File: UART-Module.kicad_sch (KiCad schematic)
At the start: 10 parts, among them J4 DE9_Receptacle_MountingHoles, Q2 1.8432, U1 74HC02, U2 74HC21, U3 W65C21N, U5 R65C51

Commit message: revise components
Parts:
- removed C1: 1uF, Capacitor_SMD:C_0805_2012Metric, symbol Device:C
- removed U3: W65C21N, Package_DIP:DIP-40_W15.24mm, symbol Interface:6821

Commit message: complete traces
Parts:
- C1: renamed from C2; footprint Capacitor_SMD:C_0805_2012Metric -> Capacitor_SMD:C_0805_2012Metric_Pad1.18x1.45mm_HandSolder
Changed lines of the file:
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@@
   (symbol (lib_id "Device:C") (at 118.11 129.54 270) (unit 1)
     (in_bom yes) (on_board yes) (dnp no) (fields_autoplaced)
-    (property "Reference" "C2" (at 118.11 122.174 90)
+    (property "Reference" "C1" (at 118.11 122.174 90)
       (effects (font (size 1.27 1.27)))
     )
@@
       (effects (font (size 1.27 1.27)))
     )
-    (property "Footprint" "Capacitor_SMD:C_0805_2012Metric" (at 114.3 130.5052 0)
+    (property "Footprint" "Capacitor_SMD:C_0805_2012Metric_Pad1.18x1.45mm_HandSolder" (at 114.3 130.5052 0)
       (effects (font (size 1.27 1.27)) hide)
     )
@@
       (project "UART-Module"
         (path "/1f20a268-715c-40e1-b980-8678b0e31942"
-          (reference "C2") (unit 1)
+          (reference "C1") (unit 1)
         )
       )
@@
       (project "UART-Module"
         (path "/1f20a268-715c-40e1-b980-8678b0e31942"
-          (reference "C3") (unit 1)
-        )
-      )
+          (reference "C2") (unit 1)
+        )
+      )

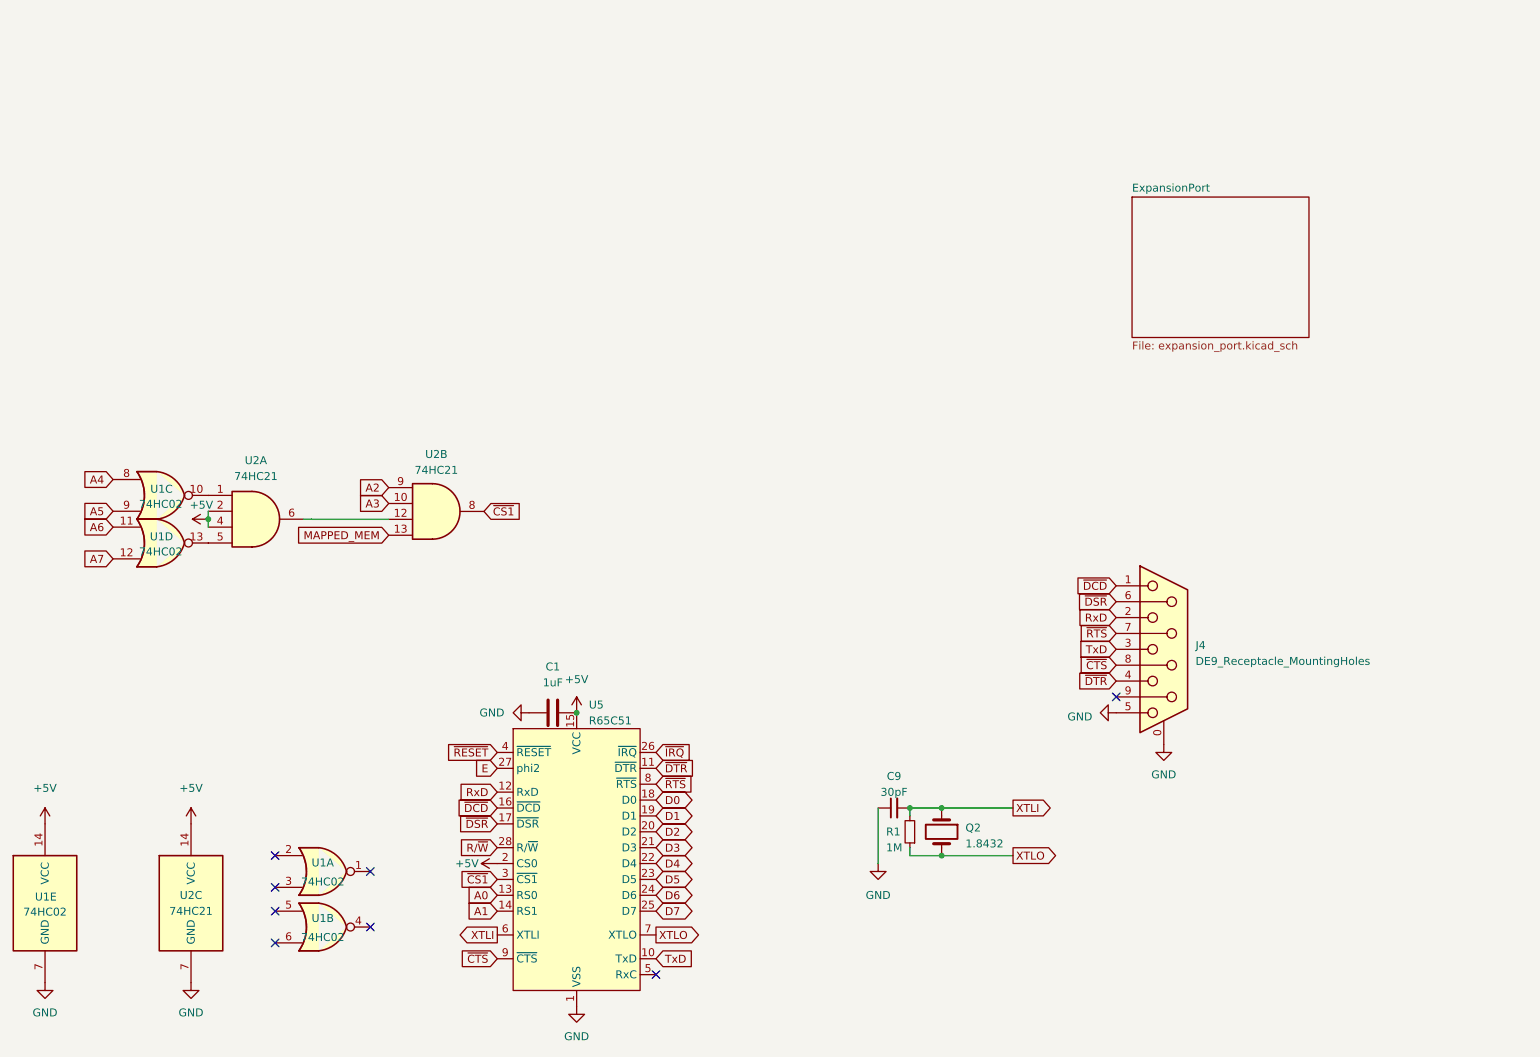
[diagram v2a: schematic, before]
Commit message: fix chip select
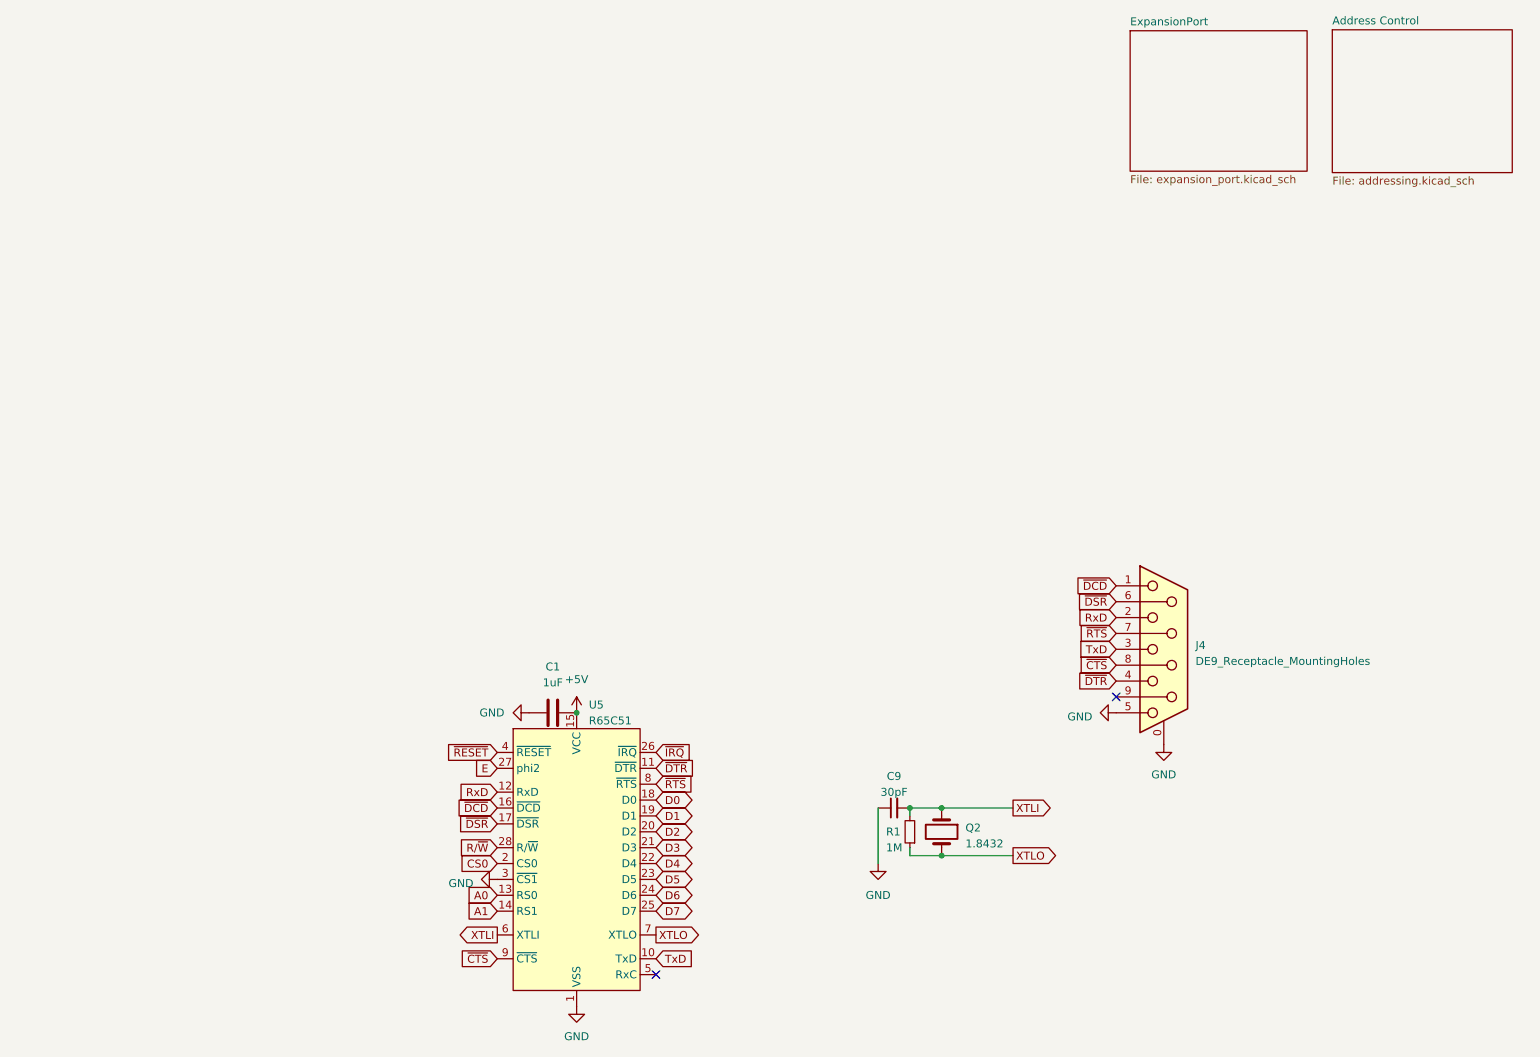
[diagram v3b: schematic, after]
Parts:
- removed U1: 74HC02, Package_SO:SO-14_3.9x8.65mm_P1.27mm, symbol 74xx:74LS02
- removed U2: 74HC21, Package_SO:SO-14_3.9x8.65mm_P1.27mm, symbol 74xx:74LS21
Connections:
- net ~{CS1} is gone; now on net GND: U5.3 (~{CS1})
- net +5V: no longer U5.2 (CS0)
- new net CS0: U5.2 (CS0)
- no-connect marks 8 -> 2
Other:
- added sheet Address Control (addressing.kicad_sch)

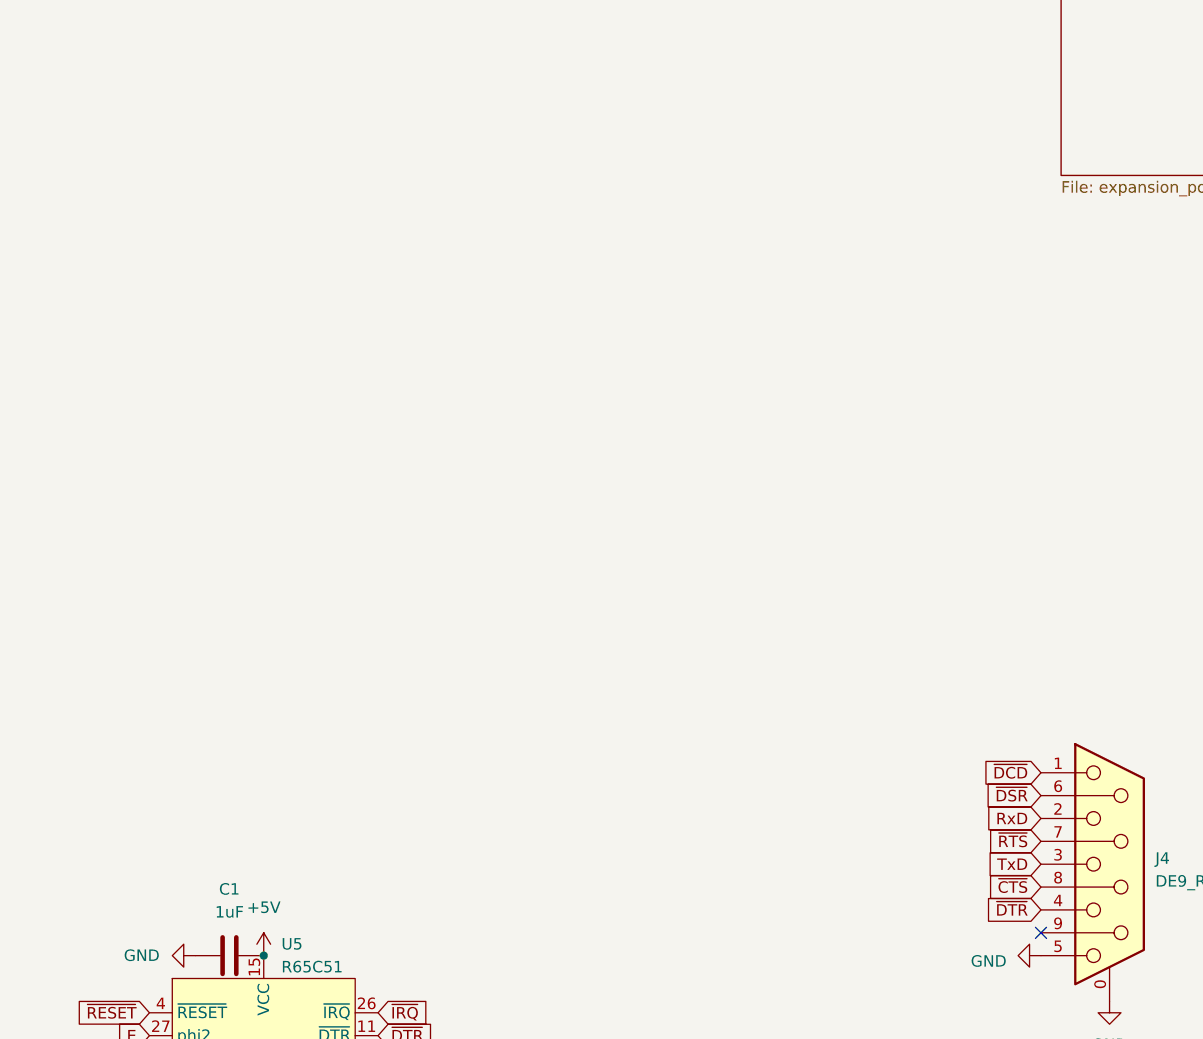
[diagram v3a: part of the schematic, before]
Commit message: add max232 for correct serial voltages
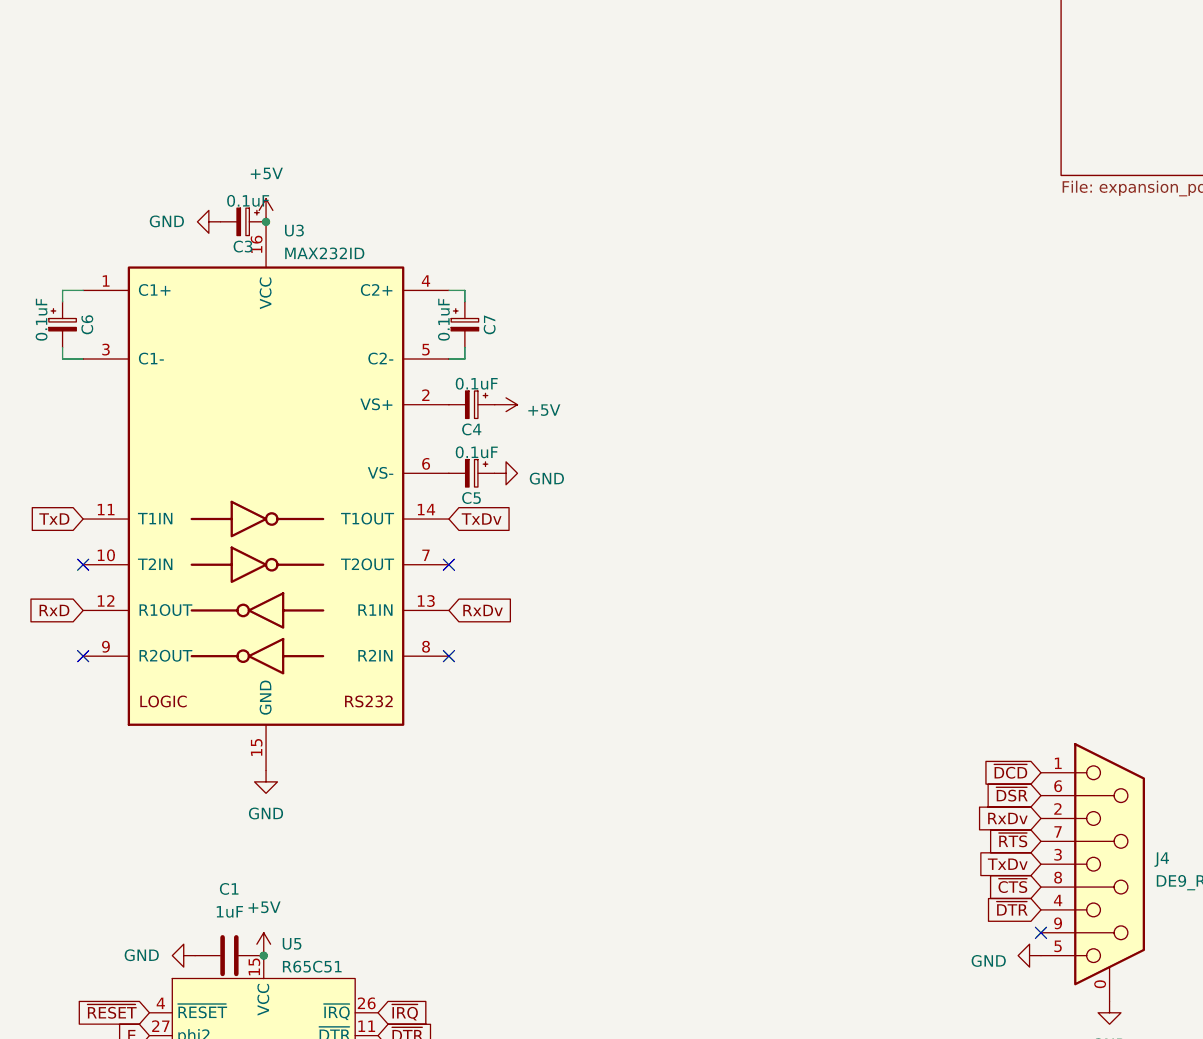
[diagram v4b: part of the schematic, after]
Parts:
- added C3, C4, C5, C6, C7: 0.1uF, Capacitor_THT:CP_Radial_Tantal_D4.5mm_P5.00mm, symbol Device:C_Polarized_Small
- added U3: MAX232ID, Package_SO:SOIC-16W_7.5x10.3mm_P1.27mm, symbol Interface_UART:MAX232
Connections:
- net +5V: now also C3.1, C4.1, U3.16 (VCC)
- net GND: now also C3.2, C5.1, U3.15 (GND)
- net RxD: now also U3.12 (R1OUT); no longer J4.2
- net TxD: now also U3.11 (T1IN); no longer J4.3
- new net: C6.1, U3.1 (C1+)
- new net: C6.2, U3.3 (C1-)
- new net: C4.2, U3.2 (VS+)
- new net: C7.1, U3.4 (C2+)
- new net: C7.2, U3.5 (C2-)
- new net: C5.2, U3.6 (VS-)
- new net RxDv: J4.2, U3.13 (R1IN)
- new net TxDv: J4.3, U3.14 (T1OUT)
- no-connect marks 2 -> 6

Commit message: fix footprint for U3
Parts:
- U3: footprint Package_SO:SOIC-16W_7.5x10.3mm_P1.27mm -> Package_SO:SOIC-16_4.55x10.3mm_P1.27mm
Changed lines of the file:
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@@
 (kicad_sch (version 20230121) (generator eeschema)
   (paper "A4")
+  (title_block
+    (date "2023-05-02")
+    (rev "1.2")
+  )
   (junction (at 121.92 129.54) (diameter 0) (color 0 0 0 0)
   )
@@
       (effects (font (size 1.27 1.27)) (justify left))
     )
-    (property "Footprint" "Package_SO:SOIC-16W_7.5x10.3mm_P1.27mm" (at 123.444 105.156 0)
-      (effects (font (size 1.27 1.27)) (justify left) hide)
-    )
+    (property "Footprint" "Package_SO:SOIC-16_4.55x10.3mm_P1.27mm" (at 123.444 105.156 0)
+      (effects (font (size 1.27 1.27)) (justify left) hide)
+    )
